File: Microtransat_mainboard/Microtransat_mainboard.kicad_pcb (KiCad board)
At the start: 2 copper layers, 41 parts, among them J1 Conn_01x08, J10 Conn_01x04, J101 12V IN, J11 Conn_01x03, J12 Conn_01x03, J13 Conn_01x03, J3 Conn_01x06, J301 ESTOP IN, J4 Conn_01x04, J5 Conn_01x05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

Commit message: Started PCB
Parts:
- removed J5: Conn_01x05, Connector_PinHeader_2.54mm:PinHeader_1x05_P2.54mm_Vertical
- added J2: Conn_01x04, Connector_JST:JST_XH_B4B-XH-A_1x04_P2.50mm_Vertical, F.Cu at (149.5, 77.5)
- J4: footprint Connector_PinHeader_2.54mm:PinHeader_1x04_P2.54mm_Vertical -> Connector_JST:JST_XH_B4B-XH-A_1x04_P2.50mm_Vertical
- moved J12 106.9 mm to (62.0, 135.5)
- moved J11 106.6 mm to (62.0, 127.0)
- moved J6 106.1 mm to (62.0, 118.0)
- moved J13 97.1 mm to (62.0, 109.5)
- moved J10 77.1 mm to (62.0, 78.5)
- moved J9 77.0 mm to (62.0, 71.0)
- moved A601 72.3 mm to (156.5, 44.0)
- moved J1 71.5 mm to (72.5, 109.1)
- moved D1 60.6 mm to (152.5, 57.0)
- moved A1 52.1 mm to (127.1, 114.3), turned to 180 degrees
- moved J301 44.9 mm to (124.5, 45.5)
- moved K301 44.6 mm to (119.5, 67.0), turned to 90 degrees
- moved D301 43.1 mm to (128.9, 50.0)
- moved U1 41.4 mm to (71.0, 49.5)
- moved U3 41.3 mm to (98.0, 44.0), turned to 180 degrees
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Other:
- board outline added: 110 x 110 mm

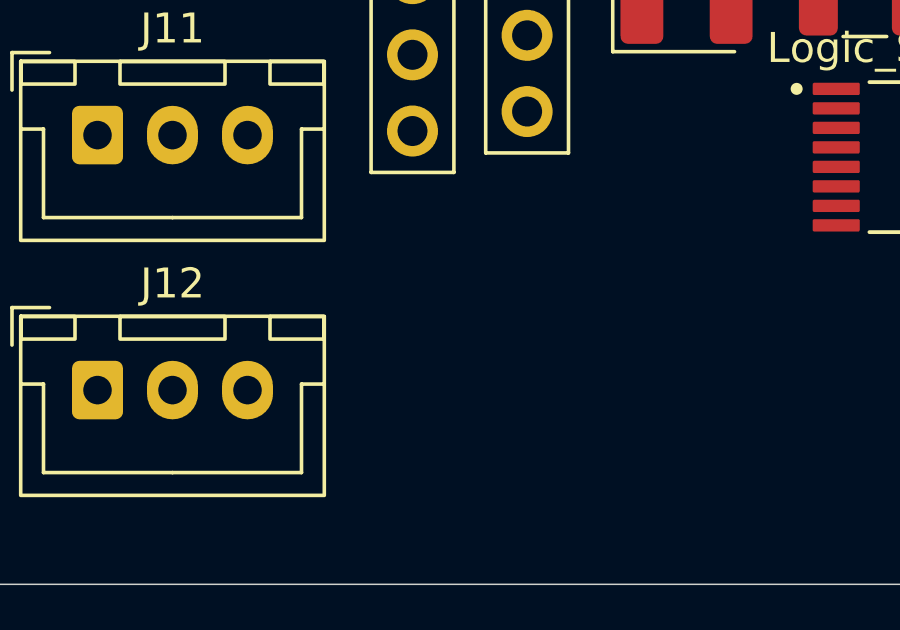
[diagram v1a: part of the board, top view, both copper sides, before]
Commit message: Added power connector for raspberry pi
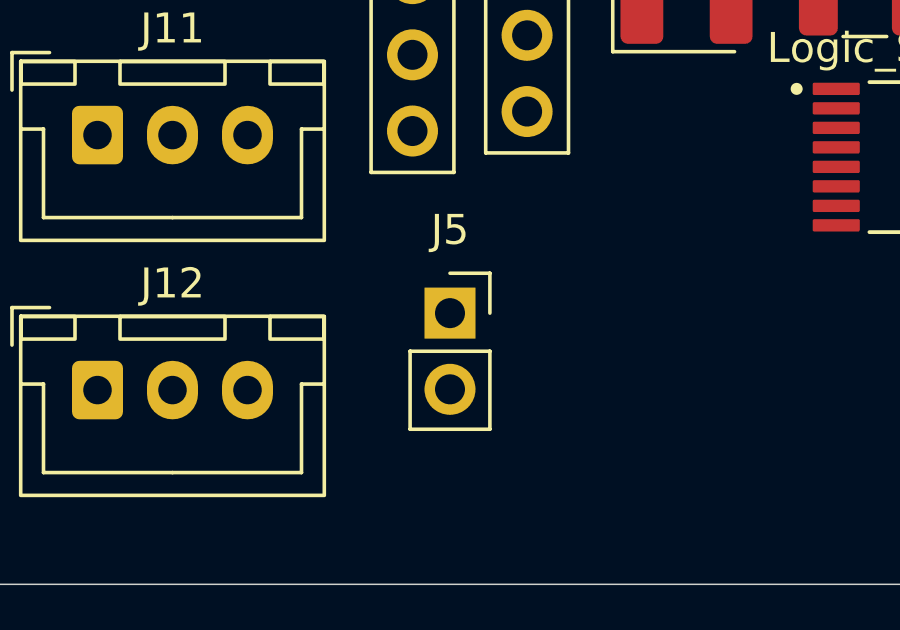
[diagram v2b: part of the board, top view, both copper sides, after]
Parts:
- added J5: Conn_01x02, Connector_PinSocket_2.54mm:PinSocket_1x02_P2.54mm_Vertical, F.Cu at (73.8, 133.0)
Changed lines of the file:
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@@
 		(embedded_fonts no)
+	)
+	(footprint "Connector_PinSocket_2.54mm:PinSocket_1x02_P2.54mm_Vertical"
+		(layer "F.Cu")
+		(at 73.75 132.96)
+		(descr "Through hole straight socket strip, 1x02, 2.54mm pitch, single row (from Kicad 4.0.7), script generated")
+		(tags "Through hole socket strip THT 1x02 2.54mm single row")
+		(property "Reference" "J5"
+			(at 0 -2.77 0)
+			(layer "F.SilkS")
+			(effects
+				(font
+					(size 1 1)
+					(thickness 0.15)
+				)
+			)
+		)
+		(property "Value" "Conn_01x02"
+			(at 0 5.31 0)
+			(layer "F.Fab")
+			(effects
+				(font
+					(size 1 1)
+					(thickness 0.15)
+				)
+			)
+		)
+		(property "Datasheet" "~"
+			(at 0 0 0)
+			(layer "F.Fab")
+			(hide yes)
+			(effects
+				(font
+					(size 1.27 1.27)
+					(thickness 0.15)
+				)
+			)
+		)
+		(property "Description" "Generic connector, single row, 01x02, script generated (kicad-library-utils/schlib/autogen/connector/)"
+			(at 0 0 0)
+			(layer "F.Fab")
+			(hide yes)
+			(effects
+				(font
+					(size 1.27 1.27)
+					(thickness 0.15)
+				)
+			)
+		)
+		(property ki_fp_filters "Connector*:*_1x??_*")
+		(sheetname "/")
+		(sheetfile "Microtransat_mainboard.kicad_sch")
+		(attr through_hole)
+		(fp_line
+			(start -1.33 1.27)
+			(end -1.33 3.87)
+			(stroke
+				(width 0.12)
+				(type solid)
+			)
+			(layer "F.SilkS")
+		)
+		(fp_line
+			(start -1.33 1.27)
+			(end 1.33 1.27)
+			(stroke
+				(width 0.12)
+				(type solid)
+			)
+			(layer "F.SilkS")
+		)
+		(fp_line
+			(start -1.33 3.87)
+			(end 1.33 3.87)
+			(stroke
+				(width 0.12)
+				(type solid)
+			)
+			(layer "F.SilkS")
+		)
+		(fp_line
+			(start 0 -1.33)
+			(end 1.33 -1.33)
+			(stroke
+				(width 0.12)
+				(type solid)
+			)
+			(layer "F.SilkS")
+		)
+		(fp_line
+			(start 1.33 -1.33)
+			(end 1.33 0)
+			(stroke
+				(width 0.12)
+				(type solid)
+			)
+			(layer "F.SilkS")
+		)
+		(fp_line
+			(start 1.33 1.27)
+			(end 1.33 3.87)
+			(stroke
+				(width 0.12)
+				(type solid)
+			)
+			(layer "F.SilkS")
+		)
+		(fp_line
+			(start -1.8 -1.8)
+			(end 1.75 -1.8)
+			(stroke
+				(width 0.05)
+				(type solid)
+			)
+			(layer "F.CrtYd")
+		)
+		(fp_line
+			(start -1.8 4.3)
+			(end -1.8 -1.8)
+			(stroke
+				(width 0.05)
+				(type solid)
+			)
+			(layer "F.CrtYd")
+		)
+		(fp_line
+			(start 1.75 -1.8)
+			(end 1.75 4.3)
+			(stroke
+				(width 0.05)
+				(type solid)
+			)
+			(layer "F.CrtYd")
+		)
+		(fp_line
+			(start 1.75 4.3)
+			(end -1.8 4.3)
+			(stroke
+				(width 0.05)
+				(type solid)
+			)
+			(layer "F.CrtYd")
+		)
+		(fp_line
+			(start -1.27 -1.27)
+			(end 0.635 -1.27)
+			(stroke
+				(width 0.1)
+				(type solid)
+			)
+			(layer "F.Fab")
+		)
+		(fp_line
+			(start -1.27 3.81)
+			(end -1.27 -1.27)
+			(stroke
+				(width 0.1)
+				(type solid)
+			)
+			(layer "F.Fab")
+		)
+		(fp_line
+			(start 0.635 -1.27)
+			(end 1.27 -0.635)
+			(stroke
+				(width 0.1)
+				(type solid)
+			)
+			(layer "F.Fab")
+		)
+		(fp_line
+			(start 1.27 -0.635)
+			(end 1.27 3.81)
+			(stroke
+				(width 0.1)
+				(type solid)
+			)
+			(layer "F.Fab")
+		)
+		(fp_line
+			(start 1.27 3.81)
+			(end -1.27 3.81)
+			(stroke
+				(width 0.1)
+				(type solid)
+			)
+			(layer "F.Fab")
+		)
+		(fp_text user "${REFERENCE}"
+			(at 0 1.27 90)
+			(layer "F.Fab")
+			(effects
+				(font
+					(size 1 1)
+					(thickness 0.15)
+				)
+			)
+		)
+		(pad "1" thru_hole rect
+			(at 0 0)
+			(size 1.7 1.7)
+			(drill 1)
+			(layers "*.Cu" "*.Mask")
+			(remove_unused_layers no)
+			(net 6 "+5V")
+			(pinfunction "Pin_1")
+			(pintype "passive")
+		)
+		(pad "2" thru_hole circle
+			(at 0 2.54)
+			(size 1.7 1.7)
+			(drill 1)
+			(layers "*.Cu" "*.Mask")
+			(remove_unused_layers no)
+			(net 5 "GND")
+			(pinfunction "Pin_2")
+			(pintype "passive")
+		)
+		(embedded_fonts no)
+		(model "${KICAD9_3DMODEL_DIR}/Connector_PinSocket_2.54mm.3dshapes/PinSocket_1x02_P2.54mm_Vertical.step"
+			(offset
+				(xyz 0 0 0)
+			)
+			(scale
+				(xyz 1 1 1)
+			)
+			(rotate
+				(xyz 0 0 0)
+			)
+		)
 	)
 	(footprint "LED_SMD:LED_1206_3216Metric_Pad1.42x1.75mm_HandSolder"

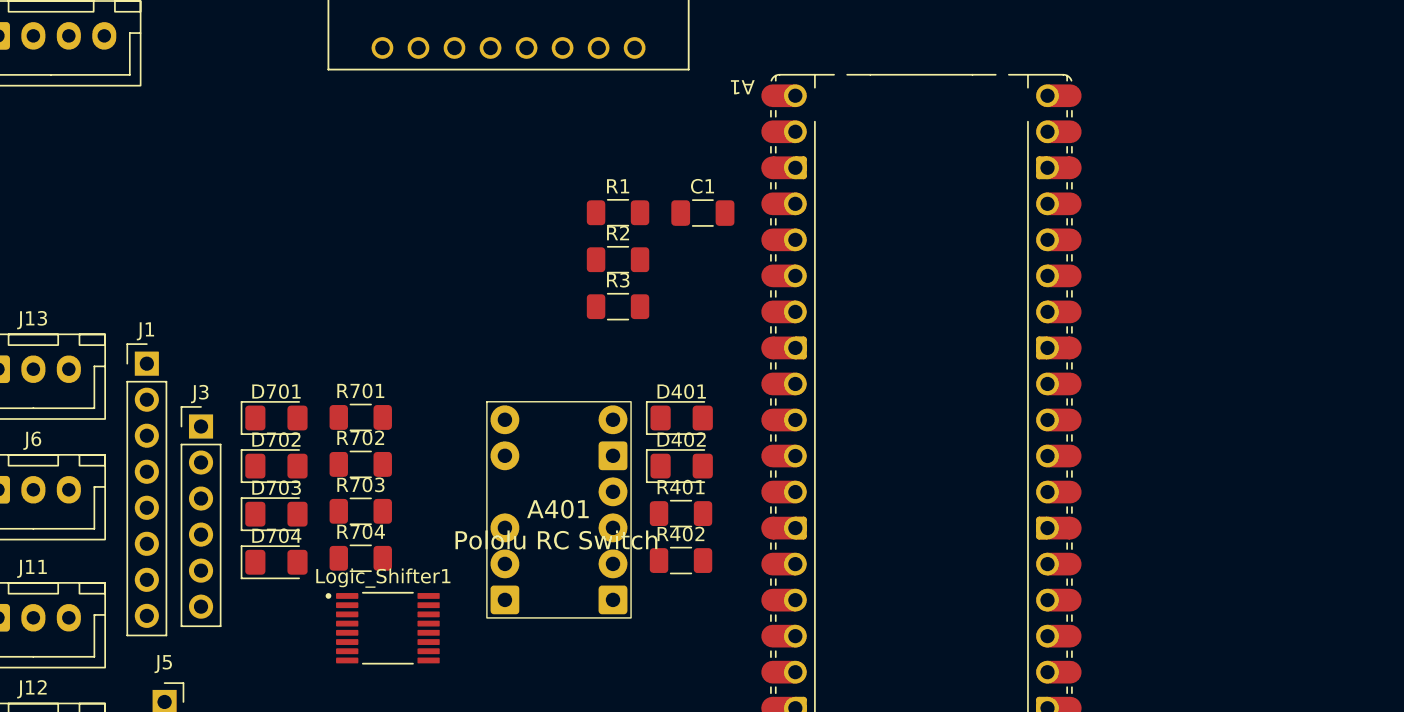
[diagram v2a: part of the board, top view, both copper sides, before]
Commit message: Added second RC switch for mode pin, added additional relay output, changed IMU to I2C
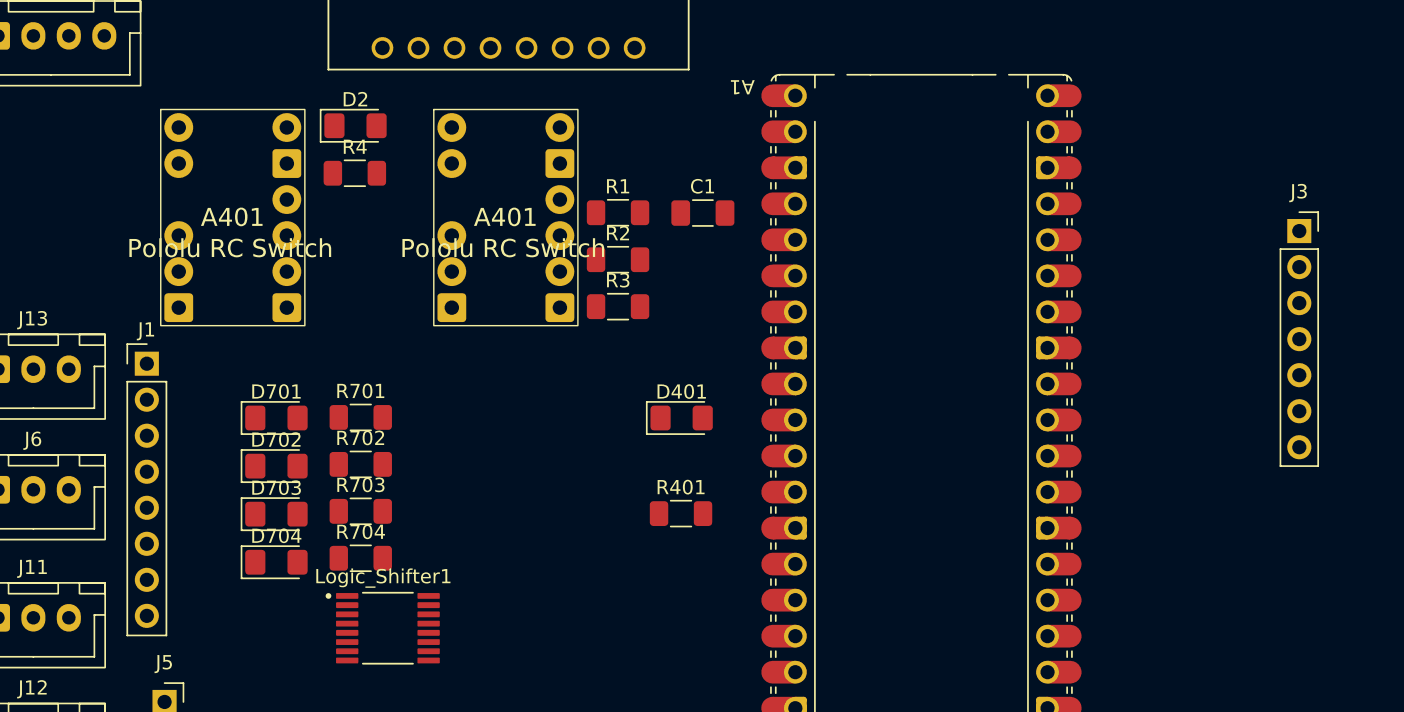
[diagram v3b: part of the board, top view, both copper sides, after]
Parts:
- removed A401: ~, Microtransat:Pololu RC Switch
- removed D402: LED, LED_SMD:LED_1206_3216Metric_Pad1.42x1.75mm_HandSolder
- removed R402: 220, Resistor_SMD:R_1206_3216Metric_Pad1.30x1.75mm_HandSolder
- added A2: ~, Microtransat:Pololu RC Switch, F.Cu at (78.4, 99.0)
- added A4: ~, Microtransat:Pololu RC Switch, F.Cu at (97.6, 99.0)
- added D2: LED, LED_SMD:LED_1206_3216Metric_Pad1.42x1.75mm_HandSolder, F.Cu at (87.2, 92.3)
- added R4: 220, Resistor_SMD:R_1206_3216Metric_Pad1.30x1.75mm_HandSolder, F.Cu at (87.2, 95.7)
- J3: value Conn_01x06 -> Conn_01x07; footprint Connector_PinHeader_2.54mm:PinHeader_1x06_P2.54mm_Vertical -> Connector_PinSocket_2.54mm:PinSocket_1x07_P2.54mm_Vertical
- moved J3 78.6 mm to (153.8, 99.8)
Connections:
- A1 pad 12: /CS0 -> /CS
- A1 pad 17: /CS1 -> /relay0
- J1 pad 5: /MODE -> /MODEIN
- J3 pad 6: GND -> /Relay Board Interface/relay0Out
- Logic_Shifter1 pad 10: unconnected-(Logic_Shifter1-B6-Pad10) -> /Relay Board Interface/relay0Out
- Logic_Shifter1 pad 7: unconnected-(Logic_Shifter1-A6-Pad7) -> /relay0
- U2 pad 2: /CS1 -> /CS
- U3 pad JP1_4: /SCLK -> /SCL
- U3 pad JP1_5: /MISO -> /SDA
- U3 pad JP2_2: +3V3 -> unconnected-(U3-P0-PadJP2_2)
- U3 pad JP2_3: +3V3 -> unconnected-(U3-P1-PadJP2_3)
- U3 pad JP2_4: +3V3 -> unconnected-(U3-~{RST}-PadJP2_4)
- U3 pad JP2_5: /MOSI -> unconnected-(U3-DI-PadJP2_5)
- U3 pad JP2_6: /CS0 -> unconnected-(U3-CS-PadJP2_6)

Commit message: moved pcb around
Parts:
- moved J5 119.9 mm to (164.0, 54.0)
- moved U1 104.4 mm to (141.5, 126.5), turned to -90 degrees
- moved Logic_Shifter1 88.4 mm to (158.5, 72.5)
- moved D701 82.9 mm to (150.0, 66.0), turned to 180 degrees
- moved J2 82.7 mm to (71.5, 105.0), turned to 90 degrees
- moved D702 82.3 mm to (150.0, 70.5), turned to 180 degrees
- moved D703 81.7 mm to (150.0, 75.0), turned to 180 degrees
- moved R3 81.6 mm to (164.0, 48.0), turned to -90 degrees
- moved D704 81.1 mm to (150.0, 79.5), turned to 180 degrees
- moved R701 73.8 mm to (144.5, 66.0), turned to 180 degrees
- moved R702 73.0 mm to (144.5, 70.5), turned to 180 degrees
- moved R703 72.3 mm to (144.5, 75.0), turned to 180 degrees
- moved R704 71.5 mm to (144.5, 79.5), turned to 180 degrees
- moved U2 58.4 mm to (150.7, 97.7), turned to 180 degrees
- moved U3 57.7 mm to (119.5, 97.5), turned to -90 degrees
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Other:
- outline, holes or cut-outs redrawn
- board text added: "macrotransat"
- board text added: "mrg"

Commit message: we did our best...
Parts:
- moved U3 35.5 mm to (155.0, 98.0)
- moved U2 25.2 mm to (125.5, 98.0)
- moved R4 5.17 mm to (74.5, 64.2)
- moved D2 5.16 mm to (74.5, 60.5)
- moved D701 2.50 mm to (147.5, 66.0), turned to 0 degrees
- moved D702 2.50 mm to (147.5, 70.5), turned to 0 degrees
- moved D703 2.50 mm to (147.5, 75.0), turned to 0 degrees
- moved D704 2.50 mm to (147.5, 79.5), turned to 0 degrees
- moved R701 2.50 mm to (142.0, 66.0)
- moved R702 2.50 mm to (142.0, 70.5)
- moved R703 2.50 mm to (142.0, 75.0)
- moved R704 2.50 mm to (142.0, 79.5)
- moved J5 1.75 mm to (164.0, 55.8), turned to 180 degrees
- moved Logic_Shifter1 1.00 mm to (157.5, 72.5)
- moved R401 0.52 mm to (96.5, 64.5), turned to 180 degrees
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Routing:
- net GND: track 0.00 -> 193.6 mm
- net /SCL: track 0.00 -> 74.4 mm
- net /SDA: track 0.00 -> 59.4 mm
- net +5V: track 0.00 -> 56.4 mm
- net Net-(D301-A): track 0.00 -> 30.0 mm
- net LOAD_HI: track 0.00 -> 28.7 mm
- net /TX0: track 0.00 -> 26.7 mm
- net /RX0: track 0.00 -> 26.7 mm
- net Net-(D301-K): track 0.00 -> 20.4 mm
- net /VREF: track 0.00 -> 13.5 mm
- net /SCLK: track 0.00 -> 11.2 mm
- net /CS: track 0.00 -> 10.1 mm
- net /blue: track 0.00 -> 9.47 mm
- net Net-(D101-K): track 0.00 -> 7.86 mm
- net /red: track 0.00 -> 7.39 mm
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
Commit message: routed the traces (maybe?)
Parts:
- added C2: 0.1u, Capacitor_SMD:C_1206_3216Metric_Pad1.33x1.80mm_HandSolder, F.Cu at (155.7, 67.1)
- added C3: 0.1u, Capacitor_SMD:C_1206_3216Metric_Pad1.33x1.80mm_HandSolder, F.Cu at (159.0, 67.1)
- added REF**: MountingHole_3.2mm_M3, MountingHole:MountingHole_3.2mm_M3, F.Cu at (164.0, 137.0)
- added REF**: MountingHole_3.2mm_M3, MountingHole:MountingHole_3.2mm_M3, F.Cu at (61.5, 137.5)
- moved R301 1.50 mm to (101.0, 41.5)
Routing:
- net +5V: track 56.4 -> 328.5 mm
- net +3V3: track 0.00 -> 188.9 mm
- net GND: track 193.6 -> 20.8 mm, vias 0 -> 17
- net /MODE: track 0.00 -> 123.2 mm, vias 0 -> 1
- net /SDA: track 59.4 -> 173.9 mm
- net /GPIO20: track 0.00 -> 110.6 mm, vias 0 -> 1
- net /SCL: track 74.4 -> 165.1 mm
- net /VREF: track 13.5 -> 103.4 mm, vias 0 -> 1
- net /yellow: track 6.07 -> 87.9 mm
- net /red: track 7.39 -> 88.6 mm
- net /blue: track 9.47 -> 83.8 mm
- net /green: track 6.80 -> 80.9 mm
- net /PWM2: track 0.00 -> 72.6 mm
- net /GPIO21: track 4.74 -> 76.0 mm, vias 0 -> 1
- net /relay0: track 0.00 -> 63.7 mm, vias 0 -> 1
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- added copper zone on B.Cu, net GND
- added copper zone on F.Cu, net GND
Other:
- outline, holes or cut-outs redrawn
- board text removed: "macrotransat"
- board text removed: "mrg"

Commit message: DRC passing
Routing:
- net +5V: track 328.5 -> 329.5 mm
- net +3V3: track 188.9 -> 189.8 mm
- net GND: vias 17 -> 18

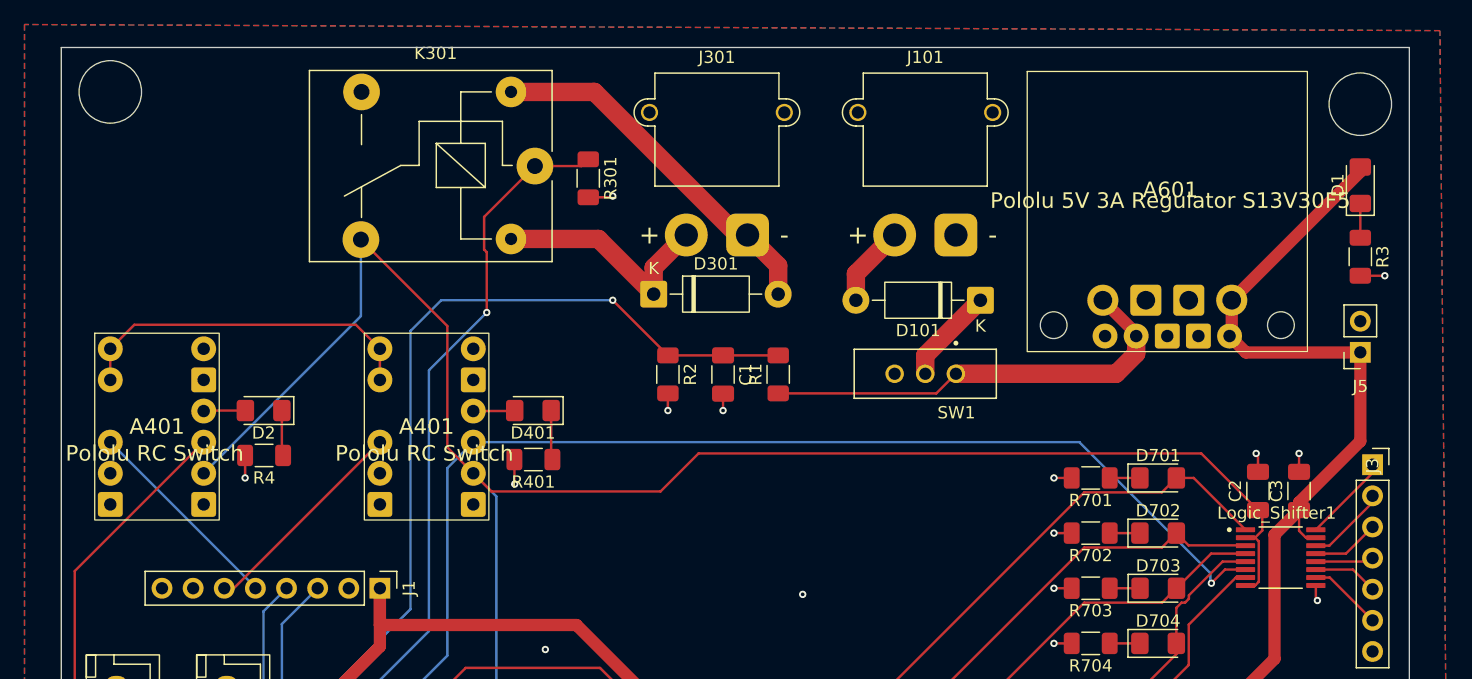
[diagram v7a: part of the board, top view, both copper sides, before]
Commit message: Fixed RC Receiver pin header
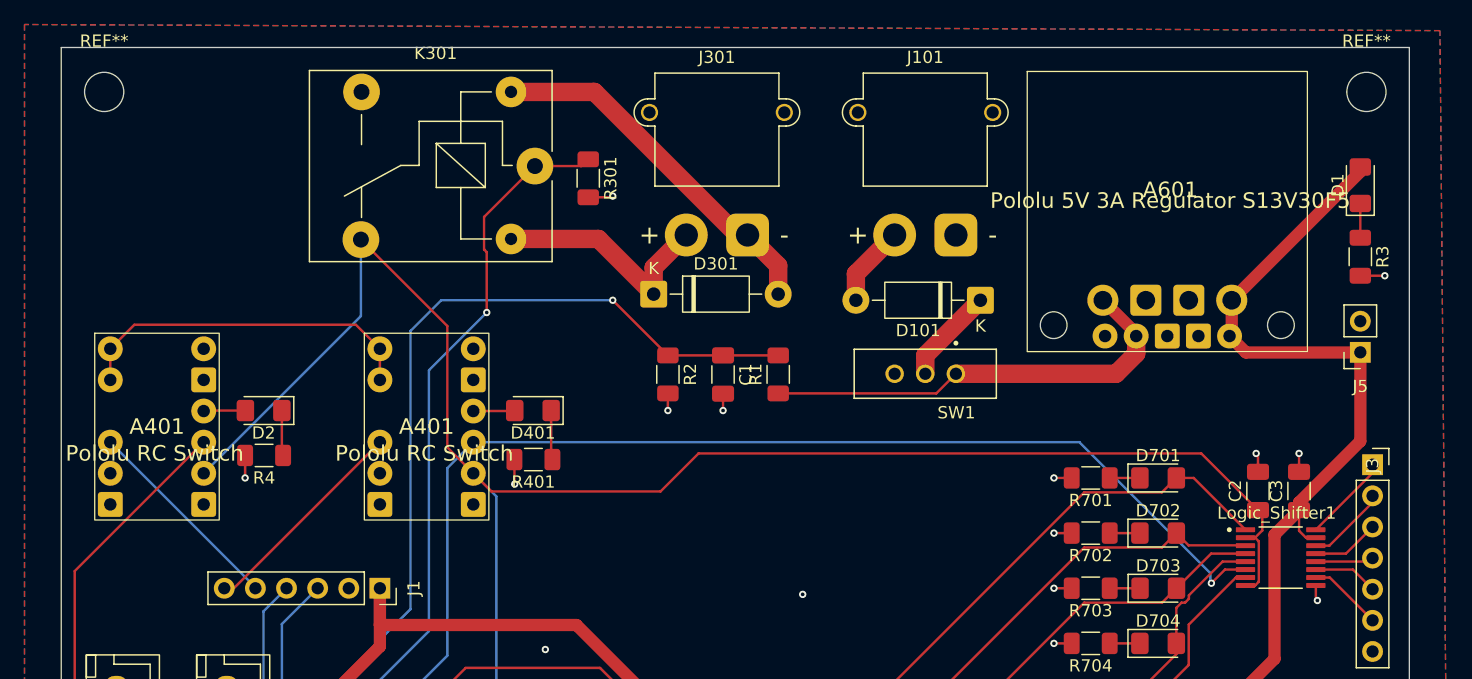
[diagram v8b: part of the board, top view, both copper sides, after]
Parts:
- added REF**: MountingHole_3.2mm_M3, MountingHole:MountingHole_3.2mm_M3, F.Cu at (164.5, 34.5)
- added REF**: MountingHole_3.2mm_M3, MountingHole:MountingHole_3.2mm_M3, F.Cu at (61.5, 34.5)
- J1: value Conn_01x08 -> Conn_01x06; footprint Connector_PinHeader_2.54mm:PinHeader_1x08_P2.54mm_Vertical -> Connector_PinSocket_2.54mm:PinSocket_1x06_P2.54mm_Vertical
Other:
- outline, holes or cut-outs redrawn
